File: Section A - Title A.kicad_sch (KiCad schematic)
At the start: 6 parts, among them J1 USB_C_Receptacle_PowerOnly_6P, J2 Conn_02x04_Odd_Even

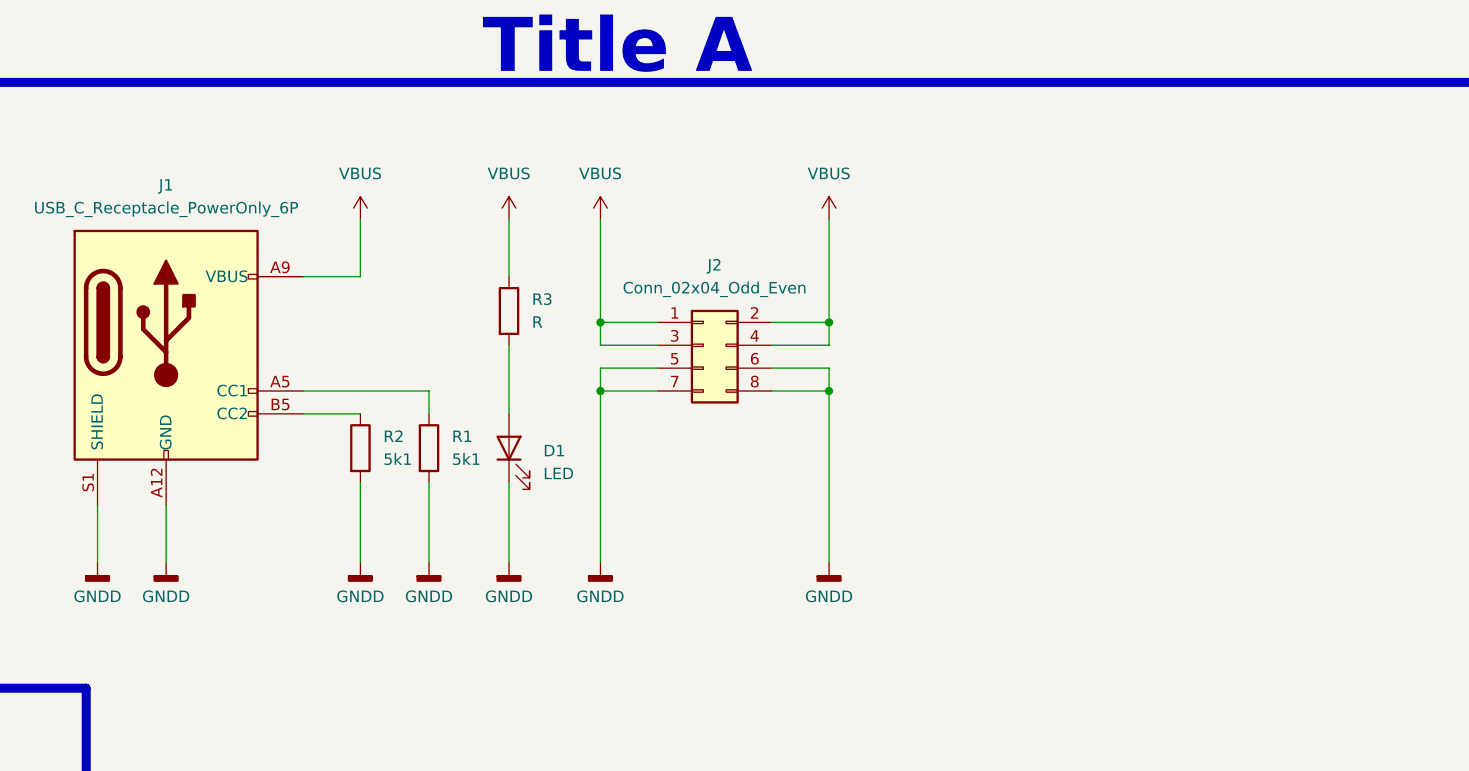
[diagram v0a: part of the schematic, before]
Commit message: Footprints, Testpoints, pwrflag
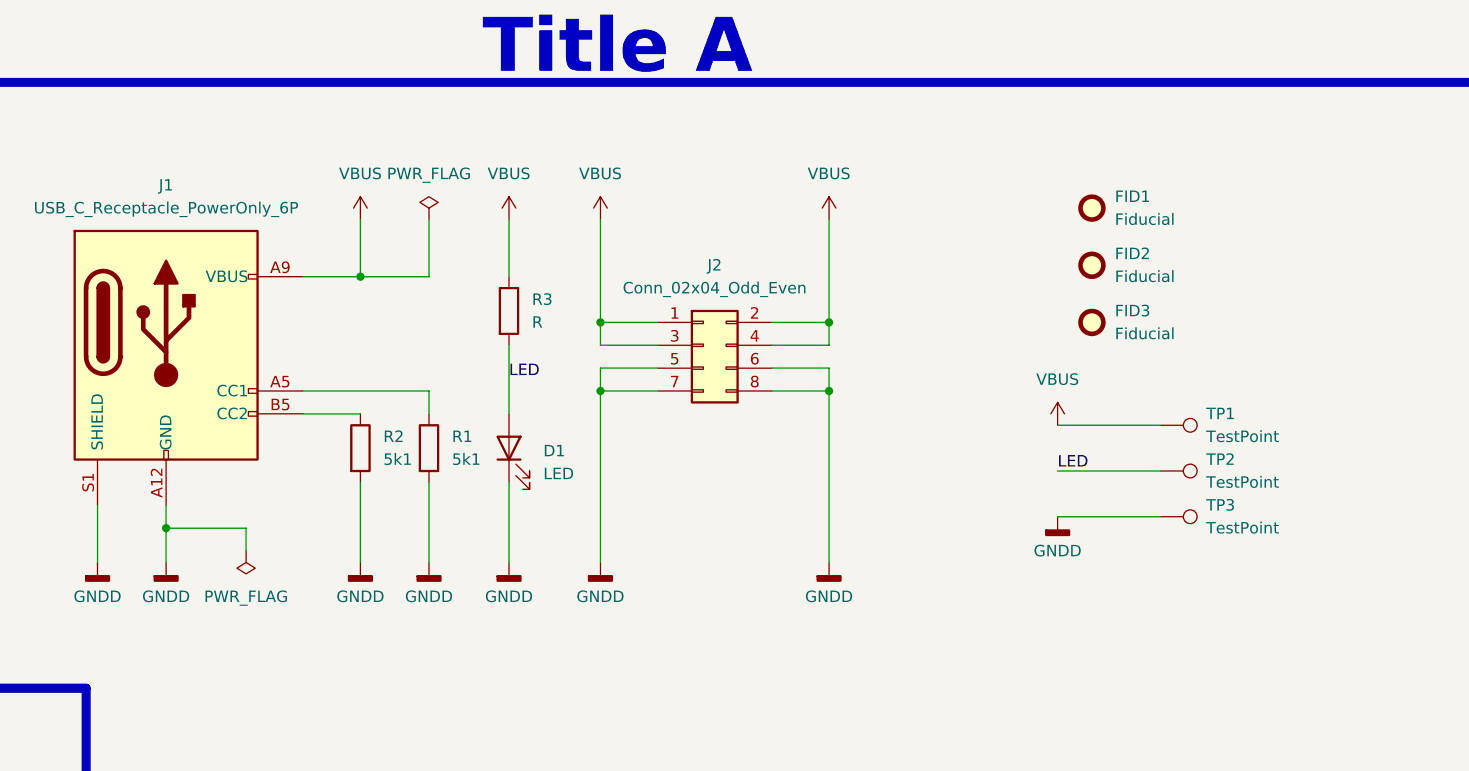
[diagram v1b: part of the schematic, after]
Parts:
- added FID1, FID2, FID3: Fiducial, Fiducial:Fiducial_1.5mm_Mask3mm, symbol Mechanical:Fiducial
- added TP1, TP2, TP3: TestPoint, TestPoint:TestPoint_Pad_D1.5mm, symbol Connector:TestPoint
- D1: footprint (none) -> LED_SMD:LED_0402_1005Metric_Pad0.77x0.64mm_HandSolder
- J1: footprint (none) -> Connector_USB:USB_C_Receptacle_GCT_USB4125-xx-x_6P_TopMnt_Horizontal
- J2: footprint (none) -> Connector_PinHeader_2.54mm:PinHeader_2x04_P2.54mm_Vertical
- R1, R2, R3: footprint (none) -> Resistor_SMD:R_0805_2012Metric_Pad1.20x1.40mm_HandSolder
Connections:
- net GNDD: now also TP3.1
- net VBUS: now also TP1.1
- net LED: now reaches D1.2 (A), R3.2
- net LED: now also TP2.1
